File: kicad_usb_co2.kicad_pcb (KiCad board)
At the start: 2 copper layers, 90 x 54 mm, 10 parts, among them SW1 SW_Push, SW2 SW_Push, U1 MH-Z14A, U2 SeeeduinoXIAO

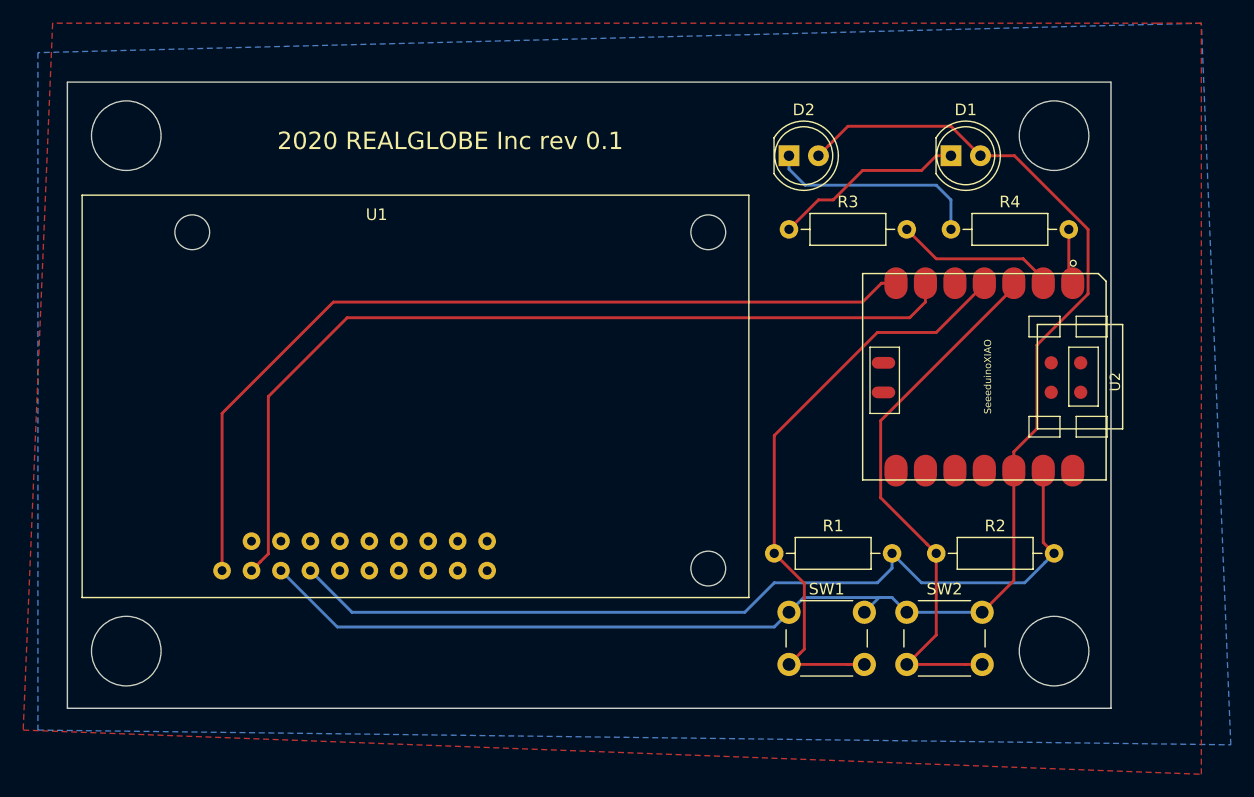
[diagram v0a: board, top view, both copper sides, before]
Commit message: 基板四隅の面取りとネジ穴をM3にした
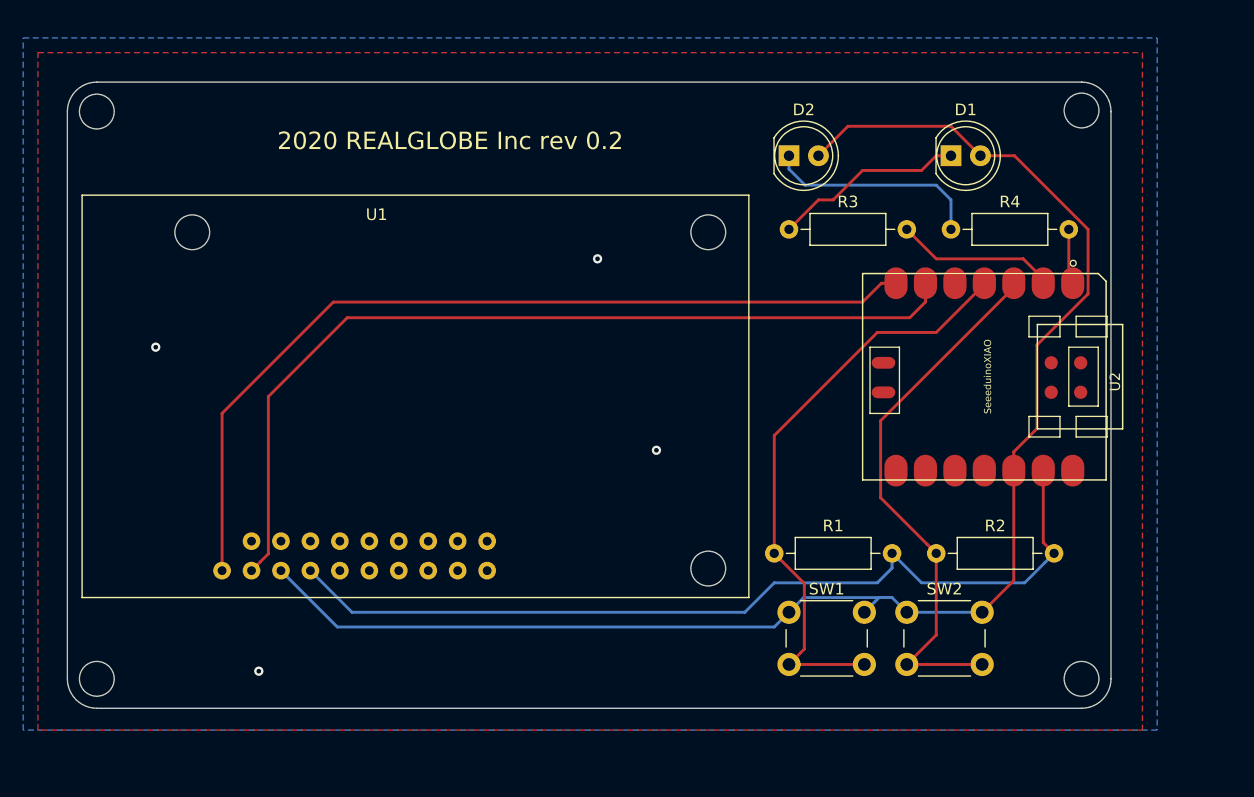
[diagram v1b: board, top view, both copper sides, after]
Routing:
- net GND: vias 0 -> 4
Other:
- outline, holes or cut-outs redrawn
- board text added: "2020 REALGLOBE Inc rev 0.2"
- board text removed: "2020 REALGLOBE Inc rev 0.1"
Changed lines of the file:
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@@
   (general
     (thickness 1.6)
-    (drawings 9)
-    (tracks 84)
+    (drawings 13)
+    (tracks 88)
     (zones 0)
     (modules 10)
@@
   (layers
     (0 F.Cu signal hide)
-    (31 B.Cu signal)
+    (31 B.Cu signal hide)
     (32 B.Adhes user)
     (33 F.Adhes user)
@@
       (net 37 "Net-(U2-Pad20)"))
   )
-  (gr_text "2020 REALGLOBE Inc rev 0.1" (at 33.02 5.08) (layer F.SilkS)
+  (gr_arc (start 87.46 2.54) (end 87.46 0) (angle 90) (layer Edge.Cuts) (width 0.05))
+  (gr_arc (start 87.46 51.46) (end 90 51.46) (angle 90) (layer Edge.Cuts) (width 0.05))
+  (gr_arc (start 2.54 51.46) (end 0 51.46) (angle -90) (layer Edge.Cuts) (width 0.05))
+  (gr_circle (center 2.54 2.54) (end 4.04 2.54) (layer Edge.Cuts) (width 0.05))
+  (gr_arc (start 2.54 2.54) (end 2.54 0) (angle -90) (layer Edge.Cuts) (width 0.05))
+  (gr_text "2020 REALGLOBE Inc rev 0.2" (at 33.02 5.08) (layer F.SilkS)
     (effects (font (size 1.5 1.5) (thickness 0.3)))
   )
-  (gr_circle (center 5.08 49.07) (end 8.08 49.07) (layer Edge.Cuts) (width 0.05))
-  (gr_circle (center 5.08 4.62) (end 8.08 4.62) (layer Edge.Cuts) (width 0.05))
-  (gr_circle (center 85.09 4.62) (end 88.09 4.62) (layer Edge.Cuts) (width 0.05))
-  (gr_circle (center 85.09 49.07) (end 88.09 49.07) (layer Edge.Cuts) (width 0.05))
-  (gr_line (start 0 54) (end 90 54) (layer Edge.Cuts) (width 0.12))
-  (gr_line (start 90 0) (end 90 54) (layer Edge.Cuts) (width 0.12))
-  (gr_line (start 0 0) (end 0 54) (layer Edge.Cuts) (width 0.12))
-  (gr_line (start 0 0) (end 90 0) (layer Edge.Cuts) (width 0.05))
+  (gr_circle (center 2.54 51.46) (end 4.04 51.46) (layer Edge.Cuts) (width 0.05))
+  (gr_circle (center 87.46 2.45) (end 88.96 2.45) (layer Edge.Cuts) (width 0.05))
+  (gr_circle (center 87.46 51.46) (end 88.96 51.46) (layer Edge.Cuts) (width 0.05))
+  (gr_line (start 2.54 54) (end 87.46 54) (layer Edge.Cuts) (width 0.05))
+  (gr_line (start 90 2.54) (end 90 51.46) (layer Edge.Cuts) (width 0.05))
+  (gr_line (start 0 2.54) (end 0 51.46) (layer Edge.Cuts) (width 0.05))
+  (gr_line (start 2.54 0) (end 87.46 0) (layer Edge.Cuts) (width 0.05))
+  (via (at 7.62 22.86) (size 0.8) (drill 0.4) (layers F.Cu B.Cu) (net 5))
+  (via (at 45.72 15.24) (size 0.8) (drill 0.4) (layers F.Cu B.Cu) (net 5))
+  (via (at 50.8 31.75) (size 0.8) (drill 0.4) (layers F.Cu B.Cu) (net 5))
+  (via (at 16.51 50.8) (size 0.8) (drill 0.4) (layers F.Cu B.Cu) (net 5))
   (segment (start 81.675002 6.35) (end 80.012792 6.35) (width 0.25) (layer F.Cu) (net 1))
   (segment (start 80.012792 6.35) (end 78.74 6.35) (width 0.25) (layer F.Cu) (net 1))
@@
     (polygon
       (pts
-        (xy -1.27 -5.08) (xy -3.81 55.88) (xy 97.79 59.69) (xy 97.79 -5.08) (xy 93.98 -5.08)
+        (xy 92.71 -2.54) (xy 92.71 55.88) (xy -2.54 55.88) (xy -2.54 -2.54)
       )
     )
@@
     (polygon
       (pts
-        (xy -2.54 -2.54) (xy -2.54 55.88) (xy 100.33 57.15) (xy 97.79 -5.08)
+        (xy 93.98 -3.81) (xy 93.98 55.88) (xy -3.81 55.88) (xy -3.81 -3.81)
       )
     )
